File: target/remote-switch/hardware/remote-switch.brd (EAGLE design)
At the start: 91.4 x 91.4 mm, 89 parts, among them IC1 MEGA8-P, IC2 LTC485N, Q2 BSS123, T1 TIC225S, T2 TIC225S, T3 TIC225S, T4 TIC225S

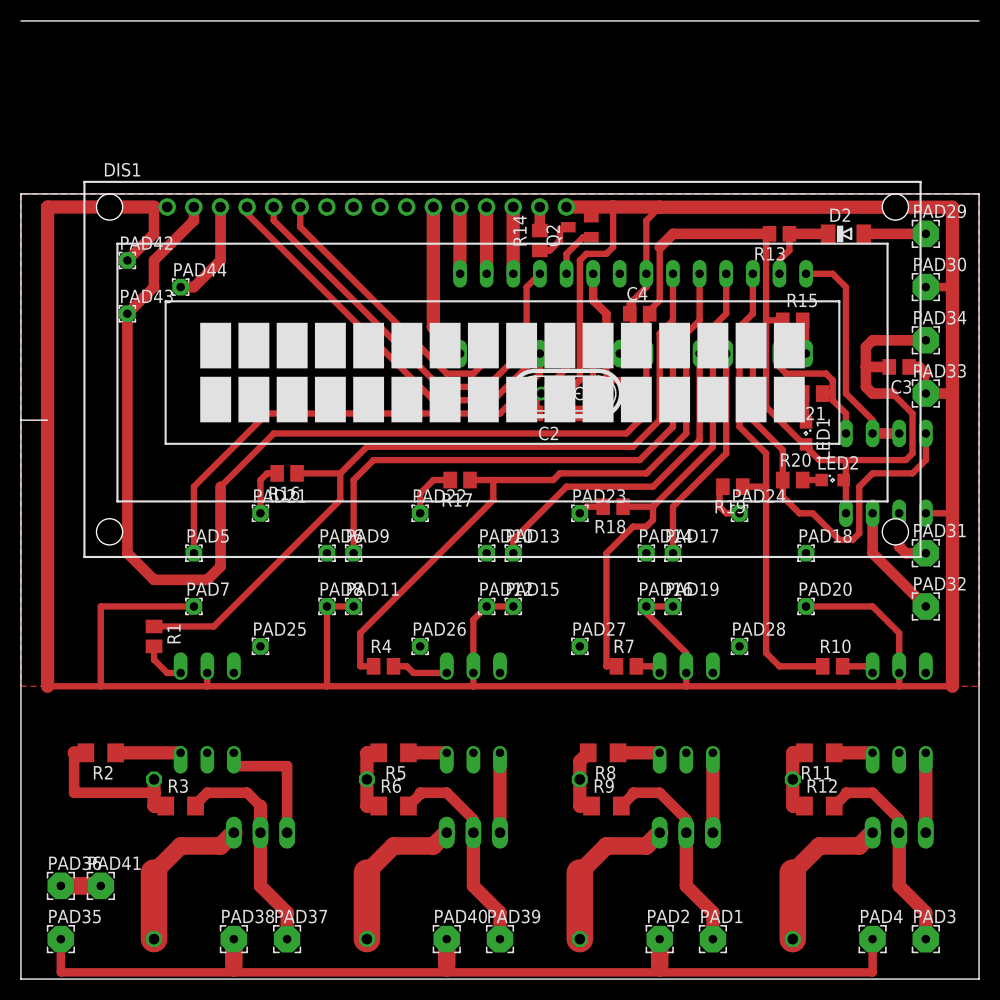
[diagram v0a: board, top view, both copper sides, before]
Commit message: remote-switch: firmware - initial revision
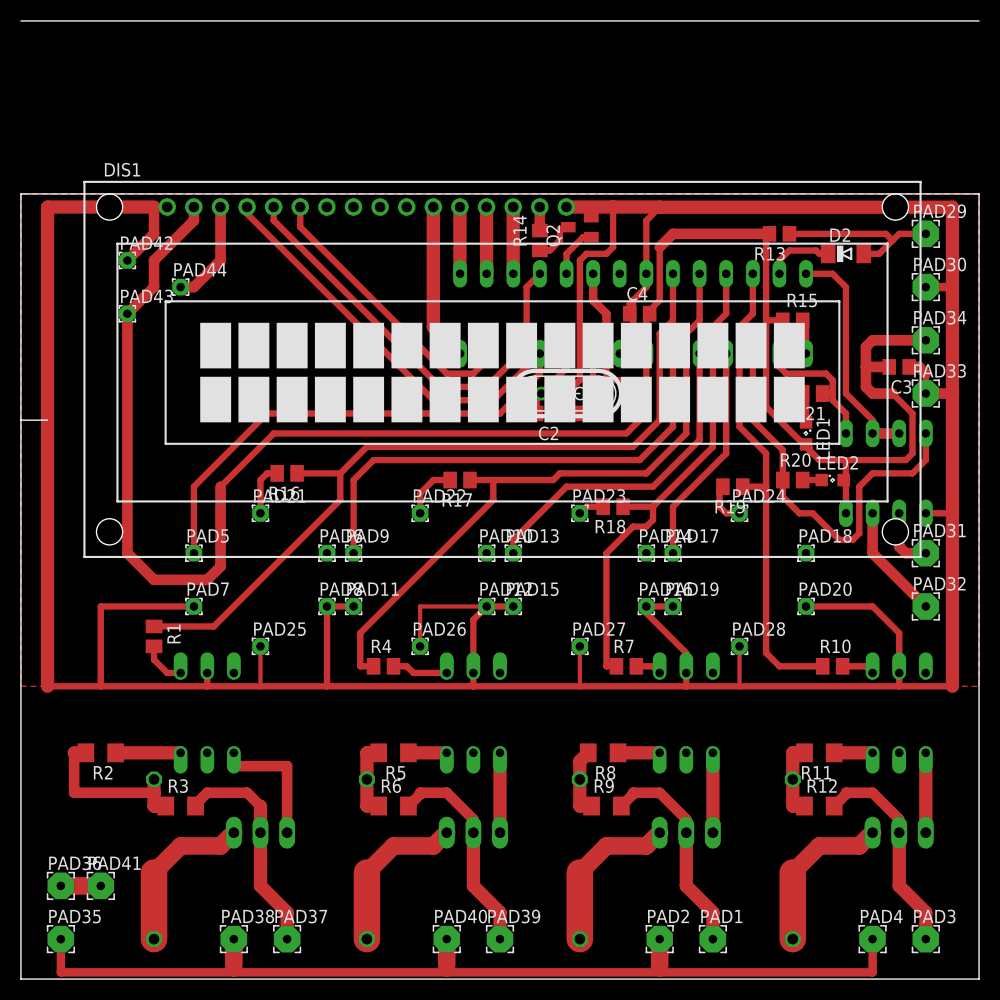
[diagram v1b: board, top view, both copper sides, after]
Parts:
- moved D2 1.91 mm to (78.7, 69.2)
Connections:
- net GND: now also PAD25.1, PAD26.1, PAD27.1, PAD28.1
- net OW: no longer R13.1
- net OWBUS: now also R13.1
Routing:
- net GND: track 354.1 -> 375.7 mm
- net OWBUS: track 5.92 -> 16.8 mm
- net OW: track 7.90 -> 6.44 mm
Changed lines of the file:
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@@
 </element>
 <element name="R13" library="rcl" package="R0805" value="1k" x="72.39" y="71.12" rot="R180"/>
-<element name="D2" library="diode" package="MINIMELF" value="" x="78.74" y="71.12"/>
+<element name="D2" library="diode" package="MINIMELF" value="" x="78.74" y="69.215"/>
 <element name="PAD29" library="wirepad" package="2,54/0,8" value="" x="86.36" y="71.12"/>
 <element name="PAD30" library="wirepad" package="2,54/0,8" value="" x="86.36" y="66.04"/>
@@
 <wire x1="43.18" y1="29.21" x2="43.18" y2="27.94" width="0.6096" layer="1"/>
 <wire x1="43.18" y1="27.94" x2="29.21" y2="27.94" width="0.6096" layer="1"/>
-<wire x1="29.21" y1="27.94" x2="17.78" y2="27.94" width="0.6096" layer="1"/>
+<wire x1="29.21" y1="27.94" x2="22.86" y2="27.94" width="0.6096" layer="1"/>
+<wire x1="22.86" y1="27.94" x2="17.78" y2="27.94" width="0.6096" layer="1"/>
 <wire x1="63.5" y1="29.21" x2="63.5" y2="27.94" width="0.6096" layer="1"/>
-<wire x1="63.5" y1="27.94" x2="43.18" y2="27.94" width="0.6096" layer="1"/>
+<wire x1="63.5" y1="27.94" x2="53.34" y2="27.94" width="0.6096" layer="1"/>
+<wire x1="53.34" y1="27.94" x2="43.18" y2="27.94" width="0.6096" layer="1"/>
 <wire x1="88.9" y1="27.94" x2="83.82" y2="27.94" width="0.6096" layer="1"/>
-<wire x1="83.82" y1="27.94" x2="63.5" y2="27.94" width="0.6096" layer="1"/>
+<wire x1="83.82" y1="27.94" x2="68.58" y2="27.94" width="0.6096" layer="1"/>
+<wire x1="68.58" y1="27.94" x2="63.5" y2="27.94" width="0.6096" layer="1"/>
 <wire x1="88.9" y1="27.94" x2="88.9" y2="44.45" width="1.27" layer="1"/>
 <wire x1="88.9" y1="44.45" x2="88.9" y2="55.88" width="1.27" layer="1"/>
@@
 <wire x1="29.21" y1="35.56" x2="29.21" y2="27.94" width="0.6096" layer="1"/>
 <wire x1="43.18" y1="29.21" x2="43.18" y2="34.29" width="0.6096" layer="1"/>
-<wire x1="43.18" y1="34.29" x2="44.45" y2="35.56" width="0.6096" layer="1"/>
+<wire x1="43.18" y1="34.29" x2="43.815" y2="34.925" width="0.6096" layer="1"/>
+<wire x1="43.815" y1="34.925" x2="44.45" y2="35.56" width="0.6096" layer="1"/>
 <wire x1="59.69" y1="35.56" x2="59.69" y2="34.925" width="0.6096" layer="1"/>
 <wire x1="59.69" y1="34.925" x2="63.5" y2="31.115" width="0.6096" layer="1"/>
@@
 <wire x1="44.45" y1="35.56" x2="46.99" y2="35.56" width="0.6096" layer="1"/>
 <wire x1="59.69" y1="35.56" x2="62.23" y2="35.56" width="0.6096" layer="1"/>
+<contactref element="PAD25" pad="1"/>
+<contactref element="PAD26" pad="1"/>
+<contactref element="PAD27" pad="1"/>
+<contactref element="PAD28" pad="1"/>
+<wire x1="22.86" y1="31.75" x2="22.86" y2="27.94" width="0.4064" layer="1"/>
+<wire x1="38.1" y1="31.75" x2="38.1" y2="35.56" width="0.4064" layer="1"/>
+<wire x1="38.1" y1="35.56" x2="43.815" y2="35.56" width="0.4064" layer="1"/>
+<wire x1="43.815" y1="35.56" x2="43.815" y2="34.925" width="0.4064" layer="1"/>
+<wire x1="53.34" y1="31.75" x2="53.34" y2="27.94" width="0.4064" layer="1"/>
+<wire x1="68.58" y1="31.75" x2="68.58" y2="27.94" width="0.4064" layer="1"/>
 </signal>
 <signal name="VCC">
@@
 <signal name="OW">
 <contactref element="IC1" pad="27"/>
-<contactref element="R13" pad="1"/>
 <contactref element="D2" pad="C"/>
-<wire x1="77.04" y1="71.12" x2="73.34" y2="71.12" width="1.016" layer="1"/>
 <wire x1="72.39" y1="68.58" x2="72.39" y2="67.31" width="0.6096" layer="1"/>
 <wire x1="72.39" y1="68.58" x2="73.34" y2="69.53" width="0.6096" layer="1"/>
-<wire x1="73.34" y1="69.53" x2="73.34" y2="71.12" width="0.6096" layer="1"/>
+<wire x1="73.34" y1="69.53" x2="75.885" y2="69.53" width="0.6096" layer="1"/>
+<wire x1="75.885" y1="69.53" x2="76.2" y2="69.215" width="0.6096" layer="1"/>
+<wire x1="76.2" y1="69.215" x2="77.04" y2="69.215" width="0.6096" layer="1"/>
 </signal>
 <signal name="RTS">
@@
 <contactref element="D2" pad="A"/>
 <contactref element="PAD29" pad="1"/>
-<wire x1="86.36" y1="71.12" x2="80.44" y2="71.12" width="1.016" layer="1"/>
+<contactref element="R13" pad="1"/>
+<wire x1="73.34" y1="71.12" x2="82.55" y2="71.12" width="0.6096" layer="1"/>
+<wire x1="80.44" y1="69.215" x2="81.915" y2="69.215" width="0.6096" layer="1"/>
+<wire x1="81.915" y1="69.215" x2="83.185" y2="70.485" width="0.6096" layer="1"/>
+<wire x1="83.185" y1="70.485" x2="82.55" y2="71.12" width="0.6096" layer="1"/>
+<wire x1="86.36" y1="71.12" x2="83.82" y2="71.12" width="0.6096" layer="1"/>
+<wire x1="83.82" y1="71.12" x2="83.185" y2="70.485" width="0.6096" layer="1"/>
 </signal>
 <signal name="N$11">
